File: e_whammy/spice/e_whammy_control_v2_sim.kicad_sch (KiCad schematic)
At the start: 34 parts, among them U1 ${SIM.PARAMS}, U2 ${SIM.PARAMS}, U3 ADG779, U4 OPEN_COLLECTOR_COMPARATOR, U5 OPEN_COLLECTOR_COMPARATOR, U6 SCHMITT_NAND, U7 SCHMITT_NOR

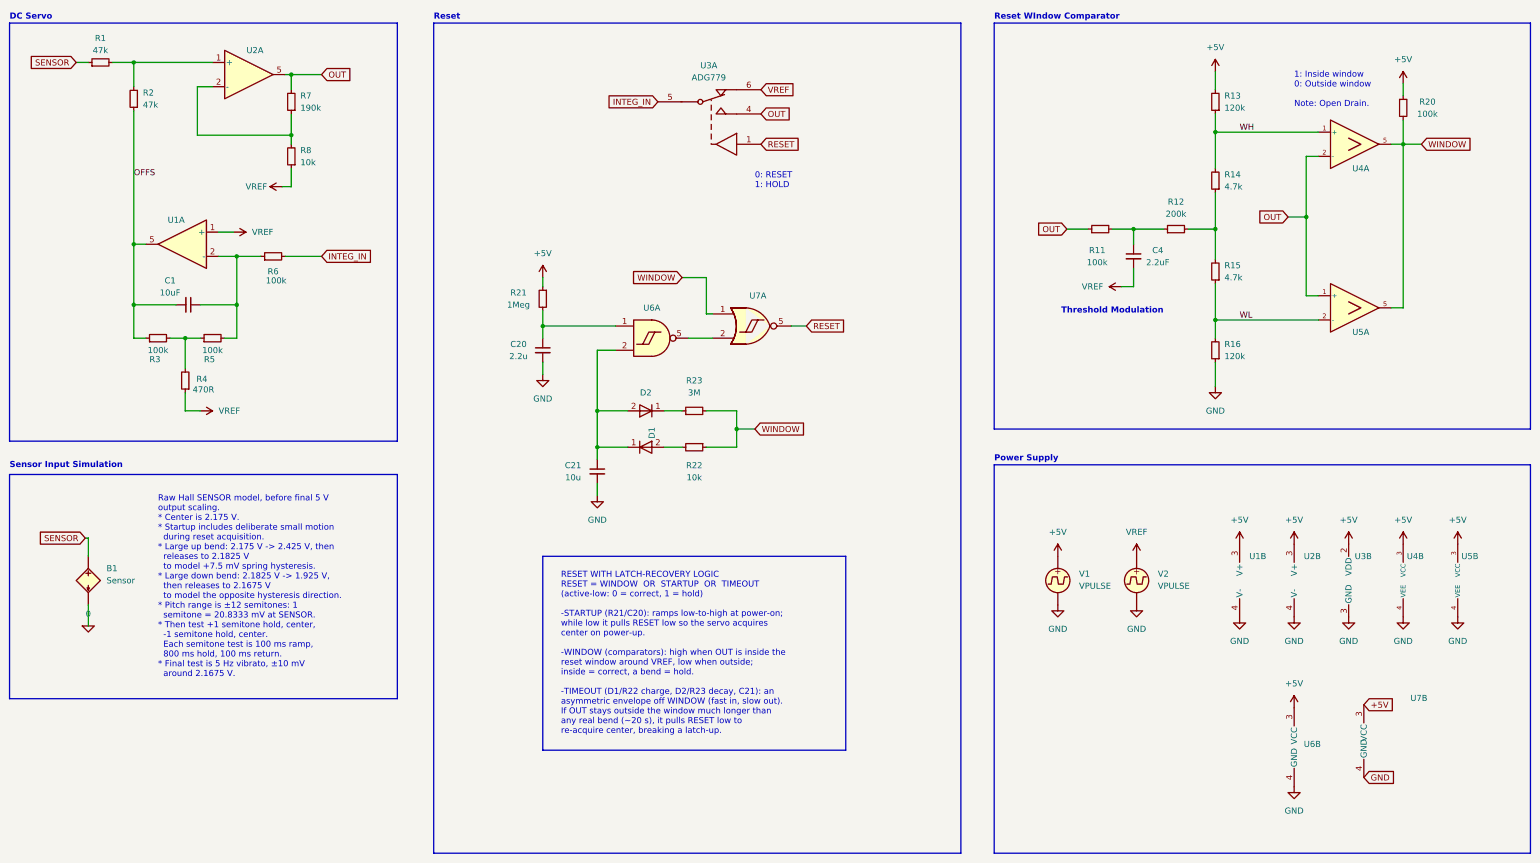
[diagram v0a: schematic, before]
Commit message: e-Whammy: collapse latch recovery to one configurable gate
RESET = WINDOW ? 0 : CTN  =  !WINDOW * CTN, realized in a single 2:1 Schmitt
mux (74x1G97-class). Deletes the startup R-C (R21/C20) and the second gate -
the timeout cap's power-on discharge supplies the startup force (startup and
latch-recovery are the same 'not recently inside the window' condition).
Full sim reproduces the metrics. Bumps pcb_common for cycfi_schmitt_mux.
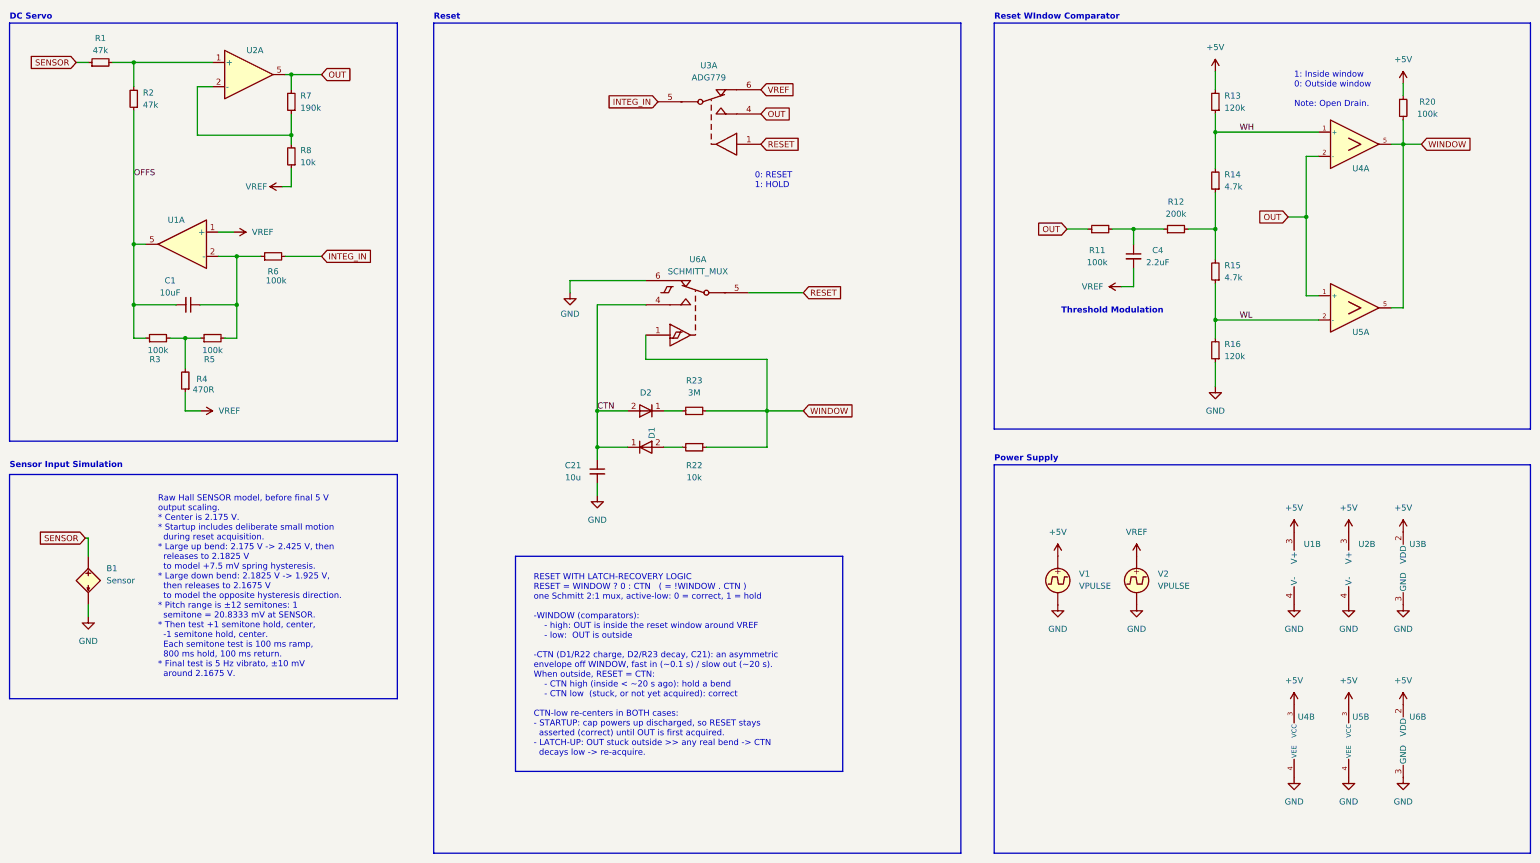
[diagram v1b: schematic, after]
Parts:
- removed C20: 2.2u, symbol Device:C_Small
- removed R21: 1Meg, symbol Device:R_Small
- removed U6: SCHMITT_NAND, symbol cycfi_spice_library:SCHMITT_NAND
- removed U7: SCHMITT_NOR, symbol cycfi_spice_library:SCHMITT_NOR
- added U6: SCHMITT_MUX, symbol cycfi_spice_library:SCHMITT_MUX
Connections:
- net 0 is gone; now on net GND: B1.2 (N-)
- net +5V: now also U6.2 (VDD)
- net GND: now also U6.3 (GND), U6.6
- net RESET: now also U6.5
- net WINDOW: now also U6.1
- net CTN: now reaches C21.1, D1.1 (K), D2.2 (A)
- net CTN: now also U6.4
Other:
- note added: "RESET WITH LATCH-RECOVERY LOGIC RESET = WINDOW ? 0 : CTN ( = !WINDOW . CTN ) one Schmitt 2:1 mux, active-low: 0 = correct, 1 = hold -WINDOW (comparators): - high: OUT is inside the reset window around VREF - low: OUT is outside -CTN (D1/R22 charge, D2/R23 decay, C21): an asymmetric envelope off WINDOW, fast in (~0.1 s) / slow out (~20 s). When outside, RESET = CTN: - CTN high (inside < ~20 s ago)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"
- note removed: "RESET WITH LATCH-RECOVERY LOGIC RESET = WINDOW OR STARTUP OR TIMEOUT (active-low: 0 = correct, 1 = hold) -STARTUP (R21/C20): ramps low-to-high at power-on; while low it pulls RESET low so the servo acquires center on power-up. -WINDOW (comparators): high when OUT is inside the reset window around VREF, low when outside; inside = correct, a bend = hold. -TIMEOUT (D1/R22 charge, D2/R23 decay, C21):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"
- moved on the sheet: U1B, U2B, U3B, U4B, U5B

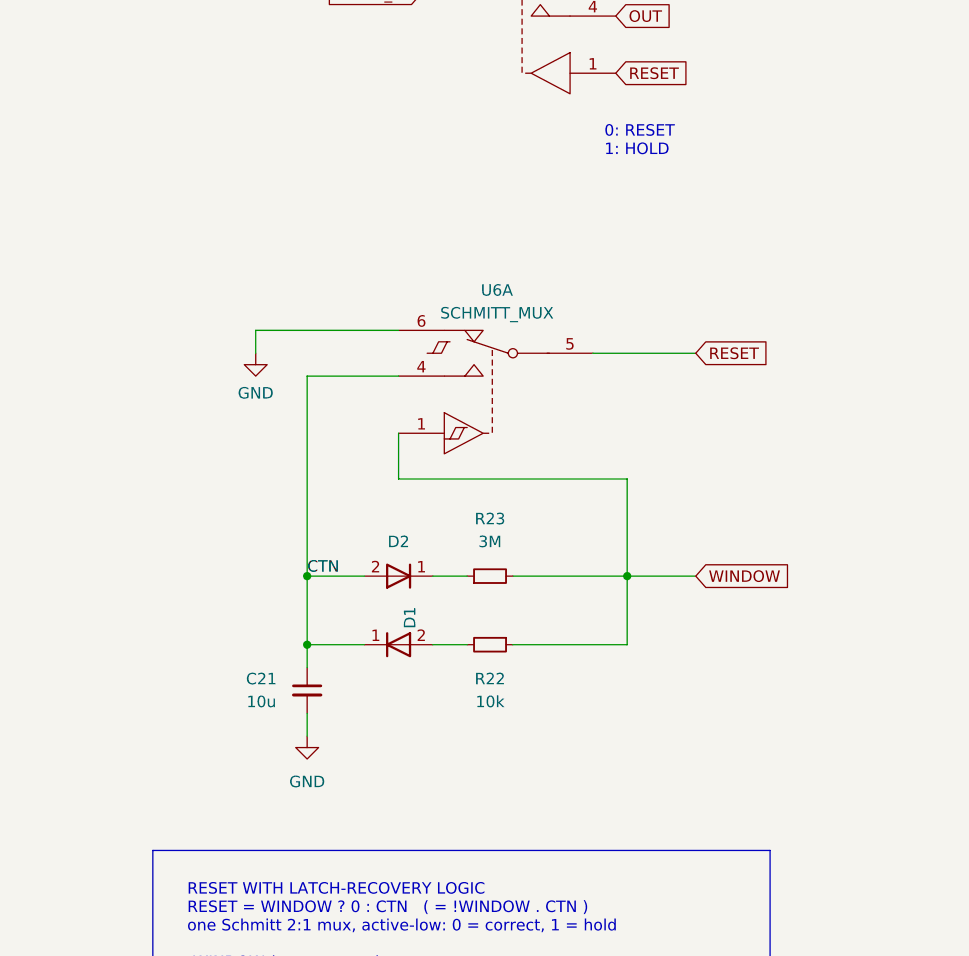
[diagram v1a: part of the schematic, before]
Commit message: e-Whammy: minor layout cleanup of v2_sim (one-gate recovery)
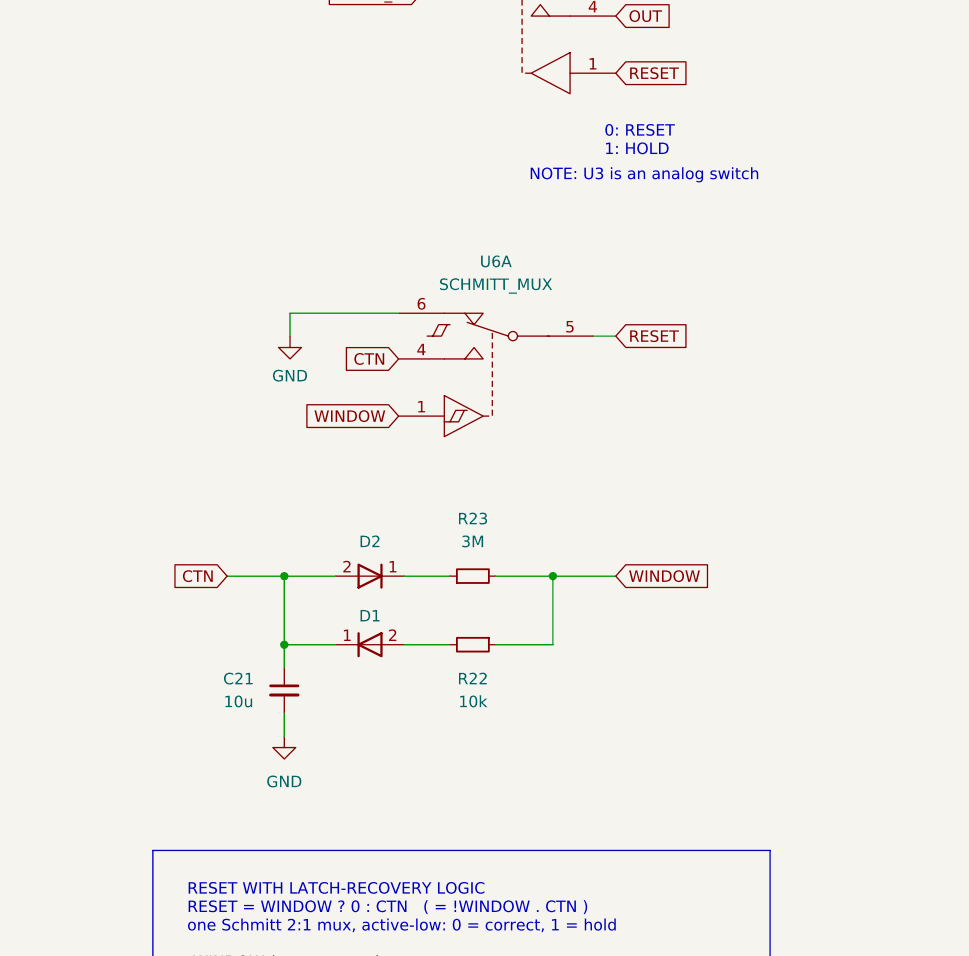
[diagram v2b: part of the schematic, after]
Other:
- note added: "NOTE: U3 is an analog switch"
- moved on the sheet: C21, D1, D2, R22, R23, U6A
